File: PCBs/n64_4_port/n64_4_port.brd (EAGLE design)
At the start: 72.9 x 73.2 mm, 45 parts, among them J5 RJ45, J6 RJ45, J7 RJ45, J8 RJ45, J9 RJ45-S-4, U1 74245, U10 MC74VHC1GT125, U2 MC74VHC1GT125, U3 MC74VHC1GT125, U4 MC74VHC1GT125, U5 MC74VHC1GT125, U7 MC74VHC1GT125, U8 MC74VHC1GT125, U9 MC74VHC1GT125

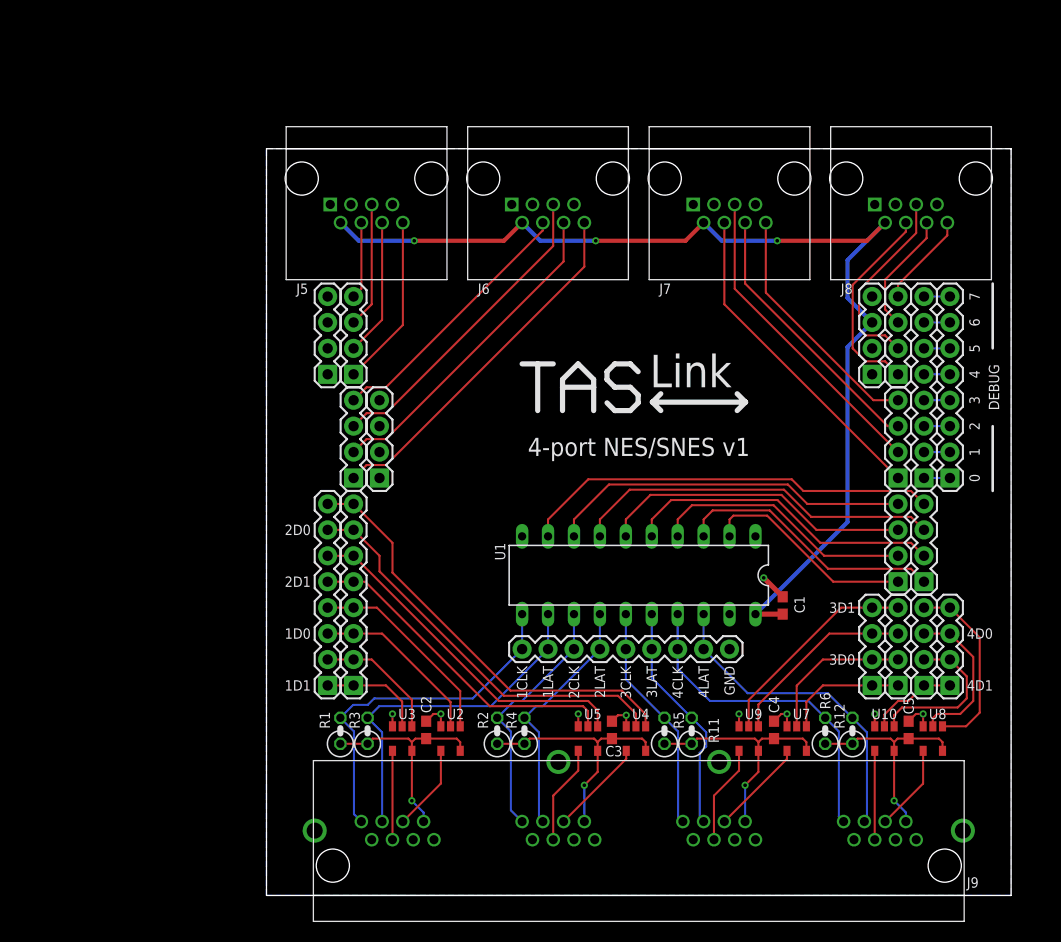
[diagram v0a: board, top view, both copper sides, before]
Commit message: N64 pcb: Schematic complete and board routed.
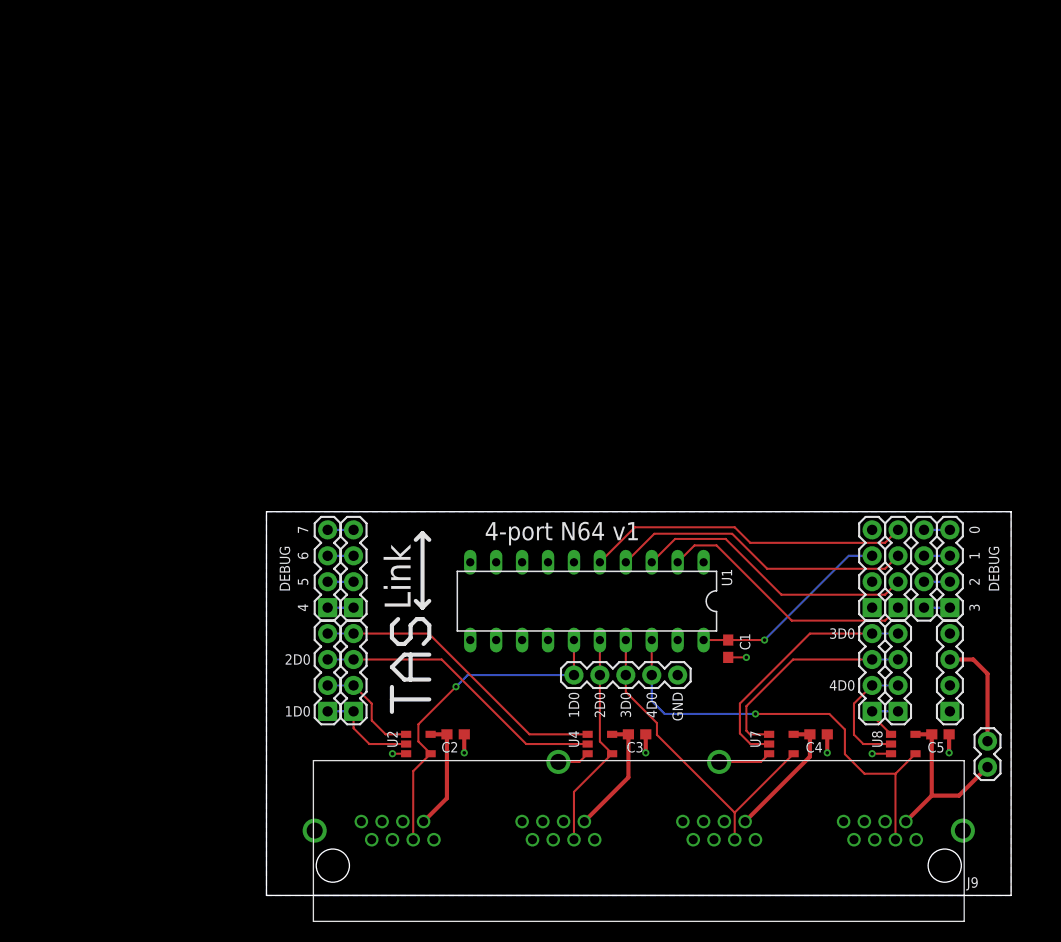
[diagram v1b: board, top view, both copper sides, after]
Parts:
- removed J5, J6, J7, J8: RJ45, TASLink:RJ45
- removed JP15, JP16, JP17, JP18, JP19, JP20: (no value), SparkFun-Connectors:1X04
- removed JP21: M09, SparkFun-Connectors:1X09
- removed JP9: (no value), SparkFun-Connectors:1X08
- removed R1, R11, R12, R2, R3, R4, R5, R6: 3.6k, rcl:0207/2V
- removed U10, U3, U5, U9: MC74VHC1GT125, TASLink:TSOP-5
- added JP10, JP3: (no value), SparkFun-Connectors:1X04
- added JP2: (no value), SparkFun-Connectors:1X05
- JP1: value (none) -> M02PTH; device SparkFun-Connectors:1X04 -> SparkFun-Connectors:1X02
- JP14, JP5, JP6: device SparkFun-Connectors:1X08 -> SparkFun-Connectors:1X04
- moved JP1 75.2 mm to (71.0, 12.6)
- moved JP6 59.8 mm to (6.35, 28.2)
- moved JP14 58.9 mm to (64.8, 28.2)
- moved JP13 57.3 mm to (67.3, 28.2)
- moved JP4 57.3 mm to (8.89, 18.0)
- moved JP7 57.3 mm to (6.35, 18.0)
- moved JP11 56.4 mm to (8.89, 28.2)
- moved JP5 53.4 mm to (62.2, 18.0)
- moved JP12 22.9 mm to (59.7, 28.2)
- moved C1 6.81 mm to (45.6, 24.2), turned to 270 degrees
- moved U1 5.68 mm to (31.8, 28.8)
- moved C4 4.39 mm to (54.4, 15.8), turned to 0 degrees
- moved JP8 3.59 mm to (59.7, 18.0)
- moved U4 3.57 mm to (33.0, 14.8), turned to 90 degrees
- moved U2 3.19 mm to (15.2, 14.8), turned to 90 degrees
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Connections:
- removed net CP1_+5V: C2.1, J9.1-2, R1.1, R3.1, U2.P$5, U3.P$5
- removed net CP1_CLOCK: J9.1-8, JP21.9, R1.2, U1.11
- removed net CP1_CLOCK_LV: JP4.4, U1.9
- removed net CP1_D0: J9.1-4, U2.P$4
- removed net CP1_D0_LV: JP14.3, JP5.3, U2.P$2
- removed net CP1_D0_OE_LV: JP14.4, JP5.4, U2.P$1
- removed net CP1_D1: J9.1-5, U3.P$4
- removed net CP1_D1_LV: JP14.1, JP5.1, U3.P$2
- removed net CP1_D1_OE_LV: JP14.2, JP5.2, U3.P$1
- removed net CP1_IODATA: J9.1-3
- removed net CP1_LATCH: J9.1-6, JP21.8, R3.2, U1.12
- removed net CP1_LATCH_LV: JP7.4, U1.8
- removed net CP2_+5V: C3.1, J9.2-2, R2.1, R4.1, U4.P$5, U5.P$5
- removed net CP2_CLOCK: J9.2-8, JP21.7, R2.2, U1.13
- removed net CP2_CLOCK_LV: JP4.3, U1.7
- removed net CP2_D0: J9.2-4, U4.P$4
- removed net CP2_D0_OE_LV: JP14.8, JP5.8, U4.P$1
- removed net CP2_D1: J9.2-5, U5.P$4
- removed net CP2_D1_LV: JP14.5, JP5.5, U5.P$2
- removed net CP2_D1_OE_LV: JP14.6, JP5.6, U5.P$1
- removed net CP2_DO_LV: JP14.7, JP5.7, U4.P$2
- removed net CP2_IODATA: J9.2-3
- removed net CP2_LATCH: J9.2-6, JP21.6, R4.2, U1.14
- removed net CP2_LATCH_LV: JP7.3, U1.6
- removed net CP3_+5V: C4.1, J9.3-2, R11.1, R5.1, U7.P$5, U9.P$5
- removed net CP3_CLOCK: J9.3-8, JP21.5, R5.2, U1.15
- removed net CP3_CLOCK_LV: JP4.2, U1.5
- removed net CP3_D0: J9.3-4, U7.P$4
- removed net CP3_D0_LV: JP15.2, JP8.2, U7.P$2
- removed net CP3_D0_OE_LV: JP15.1, JP8.1, U7.P$1
- removed net CP3_D1: J9.3-5, U9.P$4
- removed net CP3_D1_LV: JP15.4, JP8.4, U9.P$2
- removed net CP3_D1_OE_LV: JP15.3, JP8.3, U9.P$1
- removed net CP3_IODATA: J9.3-3
- removed net CP3_LATCH: J9.3-6, JP21.4, R11.2, U1.16
- removed net CP3_LATCH_LV: JP7.2, U1.4
- removed net CP4_+5V: C5.1, J9.4-2, R12.1, R6.1, U10.P$5, U8.P$5
- removed net CP4_CLOCK: J9.4-8, JP21.3, R6.2, U1.17
- removed net CP4_CLOCK_LV: JP4.1, U1.3
- removed net CP4_D0: J9.4-4, U8.P$4
- removed net CP4_D0_OE_LV: JP11.4, JP20.4, U8.P$1
- removed net CP4_D1: J9.4-5, U10.P$4
- removed net CP4_D1_LV: JP11.1, JP20.1, U10.P$2
- removed net CP4_D1_OE_LV: JP11.2, JP20.2, U10.P$1
- removed net CP4_DO_LV: JP11.3, JP20.3, U8.P$2
- removed net CP4_IODATA: J9.4-3
- removed net CP4_LATCH: J9.4-6, JP21.2, R12.2, U1.18
- removed net CP4_LATCH_LV: JP7.1, U1.2
- removed net VP1_CLOCK: J5.8, JP19.1
- removed net VP1_D0: J5.4, JP19.4
- removed net VP1_D1: J5.5, JP19.3
- removed net VP1_D2: J5.3
- removed net VP1_D3: J5.7
- removed net VP1_LATCH: J5.6, JP19.2
- removed net VP2_CLOCK: J6.8, JP17.1
- removed net VP2_D0: J6.4, JP17.4
- removed net VP2_D1: J6.5, JP17.3
- removed net VP2_D2: J6.3
- removed net VP2_D3: J6.7
- removed net VP2_LATCH: J6.6, JP17.2
- removed net VP3_CLOCK: J7.8, JP18.4
- removed net VP3_D0: J7.4, JP18.1
- removed net VP3_D1: J7.5, JP18.2
- removed net VP3_D2: J7.3
- removed net VP3_D3: J7.7
- removed net VP3_LATCH: J7.6, JP18.3
- removed net VP4_CLOCK: J8.8, JP16.4
- removed net VP4_D0: J8.4, JP16.1
- removed net VP4_D1: J8.5, JP16.2
- removed net VP4_D2: J8.3
- removed net VP4_D3: J8.7
- removed net VP4_LATCH: J8.6, JP16.3
- new net CP1_+3V3: C2.1, J9.1-2, U2.P$5
- new net CP1_DATA: J9.1-3, JP2.5, U1.15, U2.P$4
- new net CP1_DATA_IN_LV: JP3.4, U1.5
- new net CP1_DATA_OUT_LV: JP4.1, JP7.1, U2.P$2
- new net CP1_DATA_OUT_OE_LV: JP4.2, JP7.2, U2.P$1
- new net CP2_+3V3: C3.1, J9.2-2, U4.P$5
- new net CP2_DATA: J9.2-3, JP2.4, U1.16, U4.P$4
- new net CP2_DATA_IN_LV: JP3.3, U1.4
- new net CP2_DATA_OUT_LV: JP4.3, JP7.3, U4.P$2
- new net CP2_DATA_OUT_OE_LV: JP4.4, JP7.4, U4.P$1
- new net CP3_+3V3: C4.1, J9.3-2, U7.P$5
- new net CP3_DATA: J9.3-3, JP2.3, U1.17, U7.P$4
- new net CP3_DATA_IN_LV: JP3.2, U1.3
- new net CP3_DATA_OUT_LV: JP5.4, JP8.4, U7.P$2
- new net CP3_DATA_OUT_OE_LV: JP5.3, JP8.3, U7.P$1
- new net CP4_+3V3: C5.1, J9.4-2, JP1.1, U8.P$5
- new net CP4_DATA: J9.4-3, JP2.2, U1.18, U8.P$4
- new net CP4_DATA_IN_LV: JP3.1, U1.2
- new net CP4_DATA_OUT_LV: JP5.2, JP8.2, U8.P$2
- new net CP4_DATA_OUT_OE_LV: JP5.1, JP8.1, U8.P$1
- net +3V3: now also JP1.2, JP10.3; no longer J5.2, J6.2, J7.2, J8.2
- net DEBUG0: now also JP13.4, JP14.4; no longer JP6.1, JP9.1
- net DEBUG1: now also JP13.3, JP14.3; no longer JP6.2, JP9.2
- net DEBUG2: now also JP13.2, JP14.2; no longer JP6.3, JP9.3
- net DEBUG3: now also JP13.1, JP14.1; no longer JP6.4, JP9.4
- net DEBUG4: now also JP11.4, JP6.4; no longer JP6.5, JP9.5
- net DEBUG5: now also JP11.3, JP6.3; no longer JP6.6, JP9.6
- net DEBUG6: now also JP11.2, JP6.2; no longer JP6.7, JP9.7
- net DEBUG7: now also JP11.1, JP6.1; no longer JP6.8, JP9.8
- net GND: now also JP10.1, JP2.1, U1.11, U1.12, U1.13, U1.14; no longer J5.1, J6.1, J7.1, J8.1, JP1.1, JP13.1, JP21.1, U10.P$3, U3.P$3, U5.P$3, U9.P$3
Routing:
- net +3V3: track 106.0 -> 30.8 mm, vias 3 -> 1
- net CP4_DATA: track 0.00 -> 43.4 mm, vias 0 -> 1
- net CP2_D0_OE_LV: track 42.6 -> 0.00 mm
- net CP1_CLOCK_LV: track 41.1 -> 0.00 mm
- net CP2_DO_LV: track 39.8 -> 0.00 mm
- net CP2_CLOCK_LV: track 36.2 -> 0.00 mm
- net CP1_LATCH_LV: track 35.6 -> 0.00 mm
- net VP2_CLOCK: track 35.5 -> 0.00 mm
- net CP1_CLOCK: track 35.0 -> 0.00 mm
- net CP1_LATCH: track 34.6 -> 0.00 mm
- net CP2_D1_OE_LV: track 34.3 -> 0.00 mm
- net CP1_DATA: track 0.00 -> 33.2 mm, vias 0 -> 1
- net CP4_CLOCK: track 32.7 -> 0.00 mm
- net CP2_D1_LV: track 32.2 -> 0.00 mm
- net CP3_DATA: track 0.00 -> 32.1 mm
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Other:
- board size 72.9 x 73.2 mm -> 72.9 x 37.6 mm
- board text added: "4-port N64 v1"
- board text removed: "1CLK"
- board text removed: "1D1"
- board text removed: "1LAT"
- board text removed: "2CLK"
- board text removed: "2D1"
- board text removed: "2LAT"
- board text removed: "3CLK"
- board text removed: "3D1"
- board text removed: "3LAT"
- board text removed: "4-port NES/SNES v1"
- board text removed: "4CLK"
- board text removed: "4D1"
- board text removed: "4LAT"

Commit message: N64 PCB: Added controller ports with switches and mostly routed the board.
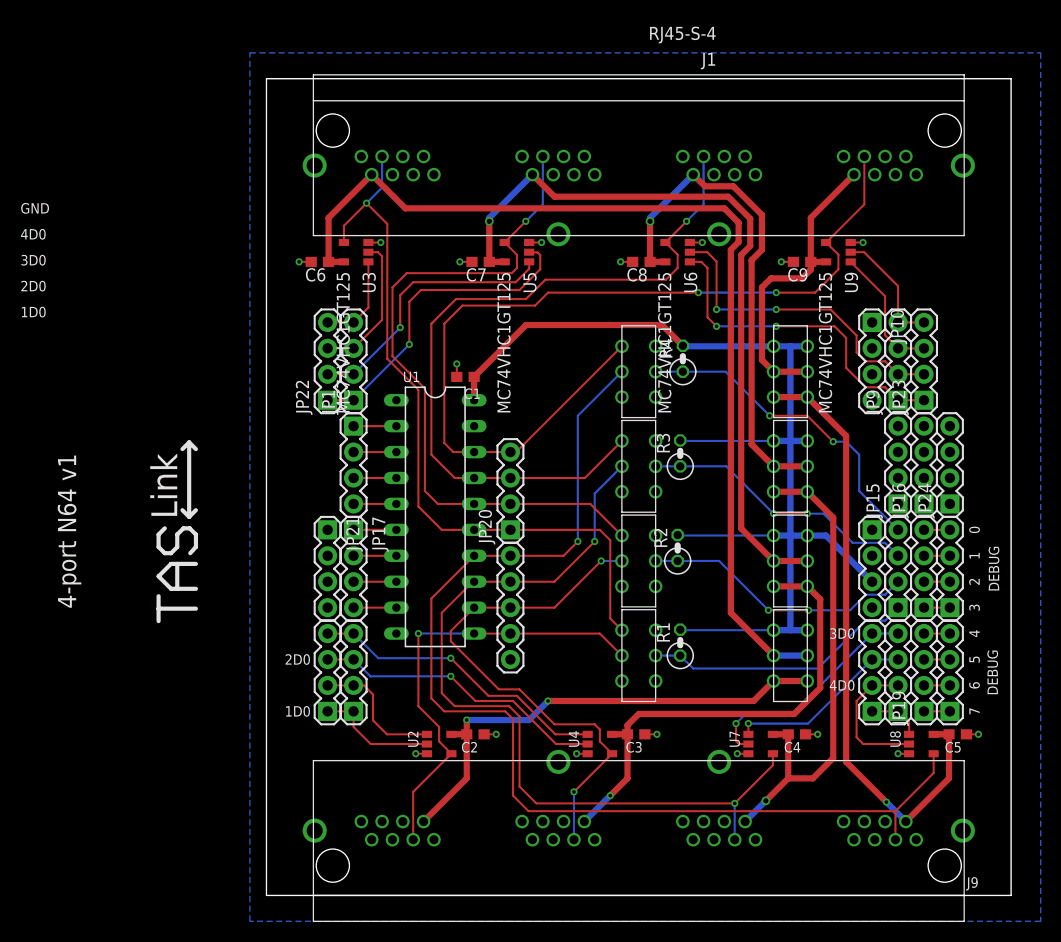
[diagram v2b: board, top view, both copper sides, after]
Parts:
- added C6, C7, C8, C9: 0.1u, rcl:C0603
- added J1: RJ45-S-4, TASLink:RJ45-S-4
- added JP15, JP16, JP17, JP19, JP20, JP21, JP22, JP23, JP24, JP9: (no value), SparkFun-Connectors:1X04
- added R1, R2, R3, R4: (no value), rcl:0207/2V
- added S1, S2, S3, S4, S5, S6, S7, S8: DPDT, TASLink:JS202011CQN
- added U3, U5, U6, U9: MC74VHC1GT125, TASLink:TSOP-5
- JP1: value M02PTH -> (none); device SparkFun-Connectors:1X02 -> SparkFun-Connectors:1X04
- moved JP1 71.8 mm to (8.89, 48.5)
- moved JP6 61.8 mm to (67.3, 18.0)
- moved JP10 38.9 mm to (59.7, 56.1), turned to 270 degrees
- moved C1 37.0 mm to (19.9, 50.8), turned to 180 degrees
- moved JP11 17.8 mm to (8.89, 46.0), turned to 270 degrees
- moved U1 17.0 mm to (16.9, 37.1), turned to 270 degrees
- moved JP2 16.5 mm to (24.3, 23.1), turned to 90 degrees
- moved JP12 7.62 mm to (59.7, 35.8), turned to 270 degrees
- moved C4 2.12 mm to (52.3, 15.8)
- moved U2 2.03 mm to (17.3, 14.8)
- moved U7 2.03 mm to (48.8, 14.8)
- moved C2 1.94 mm to (20.8, 15.8)
- moved U8 1.78 mm to (64.5, 14.8)
- moved C5 1.69 mm to (68.1, 15.8)
- moved C3 0.09 mm to (36.6, 15.8)
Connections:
- new net CP1_DIS_SIGNAL: JP3.1, R1.1, S1.5
- new net CP2_DIS_SIGNAL: JP3.2, R2.1, S3.5
- new net CP3_DIS_SIGNAL: JP3.3, R3.1, S5.5
- new net CP4_DIS_SIGNAL: JP3.4, R4.1, S7.5
- new net CTP1_+3V3: C6.1, J1.4-2, S2.2, S2.5, U3.P$5
- new net CTP1_DATA: J1.4-3, JP20.1, S1.1, U1.15, U3.P$4
- new net CTP1_DATA_IN_LV: JP11.4, U1.5
- new net CTP1_DATA_OUT_LV: JP1.3, JP22.3, U3.P$2
- new net CTP1_DATA_OUT_OE_LV: JP1.4, JP22.4, U3.P$1
- new net CTP2_+3V3: C7.1, J1.3-2, S4.2, S4.5, U5.P$5
- new net CTP2_DATA: J1.3-3, JP20.2, S3.1, U1.16, U5.P$4
- new net CTP2_DATA_IN_LV: JP11.3, U1.4
- new net CTP2_DATA_OUT_LV: JP1.1, JP22.1, U5.P$2
- new net CTP2_DATA_OUT_OE_LV: JP1.2, JP22.2, U5.P$1
- new net CTP3_+3V3: C8.1, J1.2-2, S6.2, S6.5, U6.P$5
- new net CTP3_DATA: J1.2-3, JP20.3, S5.1, U1.17, U6.P$4
- new net CTP3_DATA_IN_LV: JP11.2, U1.3
- new net CTP3_DATA_OUT_LV: JP23.2, JP9.2, U6.P$2
- new net CTP3_DATA_OUT_OE_LV: JP23.1, JP9.1, U6.P$1
- new net CTP4_+3V3: C9.1, J1.1-2, S8.2, S8.5, U9.P$5
- new net CTP4_DATA: J1.1-3, JP20.4, S7.1, U1.18, U9.P$4
- new net CTP4_DATA_IN_LV: JP11.1, U1.2
- new net CTP4_DATA_OUT_LV: JP23.4, JP9.4, U9.P$2
- new net CTP4_DATA_OUT_OE_LV: JP23.3, JP9.3, U9.P$1
- new net VP1_CLOCK: JP15.1
- new net VP1_D0: JP16.1
- new net VP1_D1: JP16.2
- new net VP1_D2: JP16.3
- new net VP1_D3: JP16.4
- new net VP1_LATCH: JP15.2
- net +3V3: now also JP24.3, R1.2, R2.2, R3.2, R4.2, S2.3, S2.6, S4.3, S4.6, S6.3, S6.6, S8.3, S8.6; no longer JP1.2, JP10.3
- net CP1_+3V3: now also S2.1, S2.4
- net CP1_DATA: now also JP2.2, S1.2, U1.11; no longer JP2.5, U1.15
- net CP1_DATA_IN_LV: now also JP17.4, U1.9; no longer JP3.4, U1.5
- net CP2_+3V3: now also S4.1, S4.4
- net CP2_DATA: now also JP2.3, S3.2, U1.12; no longer JP2.4, U1.16
- net CP2_DATA_IN_LV: now also JP17.3, U1.8; no longer JP3.3, U1.4
- net CP3_+3V3: now also S6.1, S6.4
- net CP3_DATA: now also JP2.4, S5.2, U1.13; no longer JP2.3, U1.17
- net CP3_DATA_IN_LV: now also JP17.2, U1.7; no longer JP3.2, U1.3
- net CP4_+3V3: now also S8.1, S8.4; no longer JP1.1
- net CP4_DATA: now also JP2.5, S7.2, U1.14; no longer JP2.2, U1.18
- net CP4_DATA_IN_LV: now also JP17.1, U1.6; no longer JP3.1, U1.2
- net DEBUG4: now also JP19.4; no longer JP11.4
- net DEBUG5: now also JP19.3; no longer JP11.3
- net DEBUG6: now also JP19.2; no longer JP11.2
- net DEBUG7: now also JP19.1; no longer JP11.1
- net GND: now also C6.2, C7.2, C8.2, C9.2, J1.1-1, J1.2-1, J1.3-1, J1.4-1, J1.S1, J1.S2, J1.S3, J1.S4, JP21.1, JP24.1, S1.4, S3.4, S5.4, S7.4, U3.P$3, U5.P$3, U6.P$3, U9.P$3; no longer U1.11, U1.12, U1.13, U1.14
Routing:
- net CTP1_+3V3: track 0.00 -> 97.5 mm
- net CTP4_DATA: track 0.00 -> 87.7 mm, vias 0 -> 2
- net +3V3: track 30.8 -> 111.6 mm, vias 1 -> 0
- net CTP2_+3V3: track 0.00 -> 73.4 mm, vias 0 -> 1
- net CTP3_DATA: track 0.00 -> 73.3 mm, vias 0 -> 1
- net CTP1_DATA: track 0.00 -> 71.2 mm, vias 0 -> 1
- net CTP2_DATA: track 0.00 -> 68.3 mm, vias 0 -> 1
- net CP4_DATA: track 43.4 -> 109.3 mm
- net CTP3_+3V3: track 0.00 -> 49.4 mm, vias 0 -> 1
- net CP3_DATA: track 32.1 -> 81.4 mm, vias 0 -> 2
- net CP4_+3V3: track 17.8 -> 60.7 mm, vias 0 -> 1
- net CP1_+3V3: track 11.1 -> 48.1 mm, vias 0 -> 2
- net CP2_+3V3: track 11.9 -> 46.9 mm, vias 0 -> 1
- net CP3_+3V3: track 12.8 -> 47.5 mm, vias 0 -> 1
- net CTP3_DATA_OUT_OE_LV: track 0.00 -> 33.1 mm, vias 0 -> 2
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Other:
- board size 72.9 x 37.6 mm -> 72.9 x 80 mm

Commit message: N64 PCB: Added switches, controller ports, and many other features. Layout and routing mostly complete.
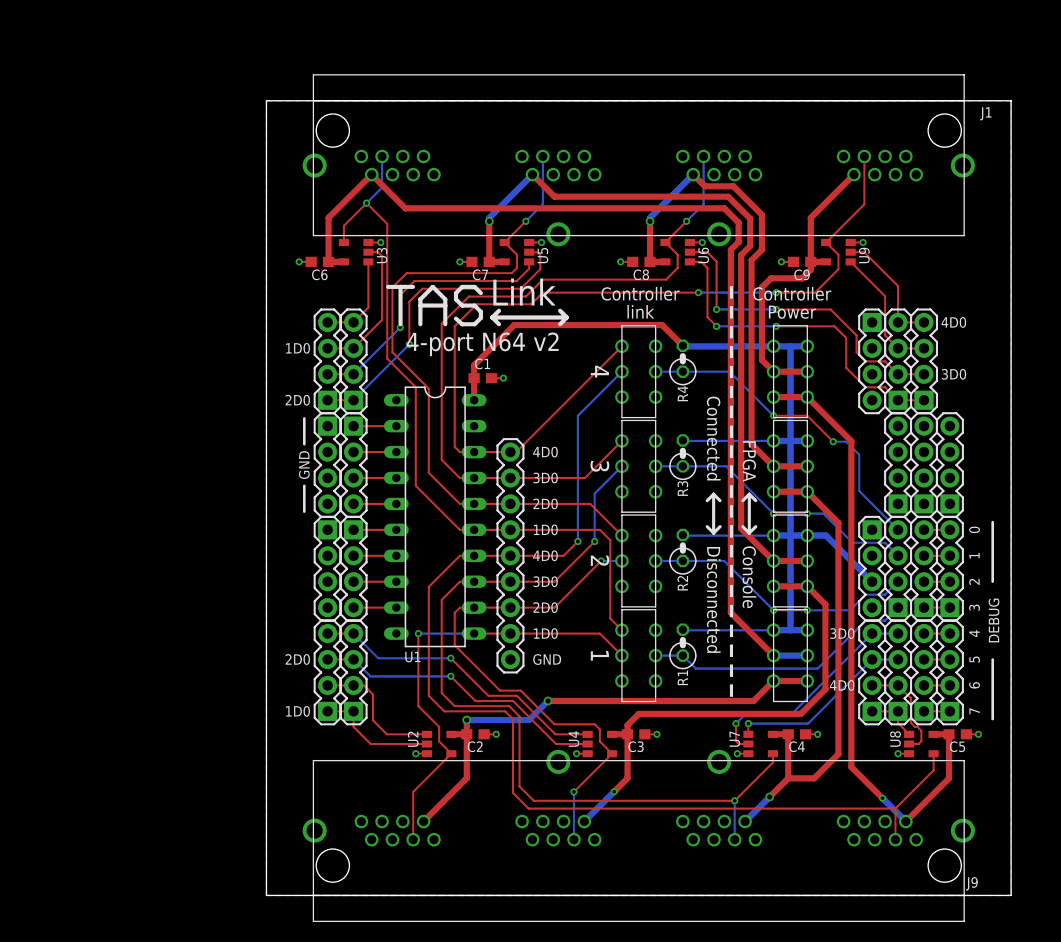
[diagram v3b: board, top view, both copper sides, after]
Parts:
- removed JP20: (no value), SparkFun-Connectors:1X04
- added JP18: M09, SparkFun-Connectors:1X09
- JP2: device SparkFun-Connectors:1X05 -> SparkFun-Connectors:1X04
- moved JP2 29.0 mm to (6.35, 46.0), turned to 270 degrees
- moved C1 1.70 mm to (21.6, 50.7), turned to 0 degrees
- moved R2 0.51 mm to (41.1, 34.0)
- moved R1 0.25 mm to (41.1, 24.8)
- moved R3 0.25 mm to (41.1, 43.3)
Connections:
- net CP1_DATA: now also JP18.2; no longer JP2.2
- net CP2_DATA: now also JP18.3; no longer JP2.3
- net CP3_DATA: now also JP18.4; no longer JP2.4
- net CP4_DATA: now also JP18.5; no longer JP2.5
- net CTP1_DATA: now also JP18.6; no longer JP20.1
- net CTP2_DATA: now also JP18.7; no longer JP20.2
- net CTP3_DATA: now also JP18.8; no longer JP20.3
- net CTP4_DATA: now also JP18.9; no longer JP20.4
- net GND: now also JP18.1, JP2.2, JP2.3, JP2.4
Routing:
- net CP4_DATA_OUT_LV: track 13.7 -> 10.4 mm
- net CTP4_DATA: track 87.7 -> 85.7 mm
- net CTP3_DATA: track 73.3 -> 71.6 mm
- net CTP2_DATA: track 68.3 -> 67.1 mm
- net CTP1_DATA: track 71.2 -> 70.2 mm
- net CP2_+3V3: track 46.9 -> 47.7 mm
- net CP4_DATA: track 109.3 -> 110.0 mm
- net CP3_DATA: track 81.4 -> 82.0 mm
- net CP2_DATA: track 51.6 -> 52.1 mm
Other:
- board size 72.9 x 80 mm -> 72.9 x 77.9 mm
- board text added: "4-port N64 v2"
- board text added: "Connected"
- board text added: "Console"
- board text added: "Controller"
- board text added: "Disconnected"
- board text added: "FPGA"
- board text added: "Power"
- board text added: "link"
- board text removed: "4-port N64 v1"
